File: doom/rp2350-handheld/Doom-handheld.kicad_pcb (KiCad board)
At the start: 2 copper layers, 160 x 100 mm, 42 parts, among them Q1 AO3401A, Q2 FS8205A, SW1 MSK12C02, U1 PIM724, U2 DW01A, U3 BQ24075RGTR

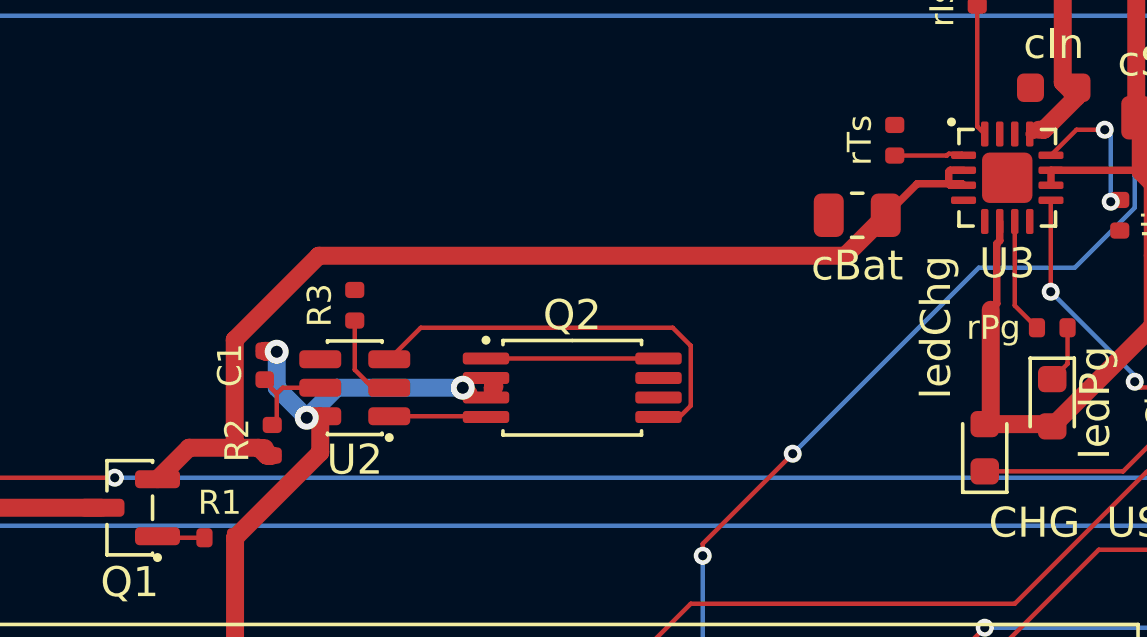
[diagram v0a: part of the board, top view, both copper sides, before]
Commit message: Boards pass check and KiCad 10's DRC again: holes in courtyards, the USB net rename
pcbkit's check now has KiCad 10's pth/npth_inside_courtyard (pcbkit be5b6955), and 13 boards
failed it. KiCad's own DRC (kicad-cli 10) reports the same holes on every one of them.

- Parts that really stand above the holes under them (a screen or a Nano on its sockets, the
  Delta-S02's КМ-6 capacitors flat under its chips, as the factory placed them): a courtyard rule
  for the pair, written to each board's .kicad_dru, so KiCad's DRC agrees.
- Real collisions moved: servo-controller's dial 3 mm up (the Nano's socket pins came out under
  it), c3-pocket's fourth M3 hole from under a cell holder to the top edge's middle, s3-rgb's
  D-pad 2 mm up (a holder's peg came through under the down key).
- v003-emu, c3-pocket, rp2040-tft, rp2350-psram, s3-rgb, teensy41: re-routed for the standard USB
  block's renamed net (usb/raw is usb/vbusIn since pcbkit 2088839e): their tracks still carried
  the old name and shorted the fuse and connector pads.
- p4-touch-7: its board file still had a courtyard for the panel the design gives none (KiCad
  reported 114 courtyard errors); written again.

Measured on the dev host: all 44 registry boards `pcbkit check` complete with 0 errors, and
kicad-cli pcb drc 0 errors on every board.

Claude-Session: https://claude.ai/code/session_018URVYF1YPgyrMNetY9yT1T
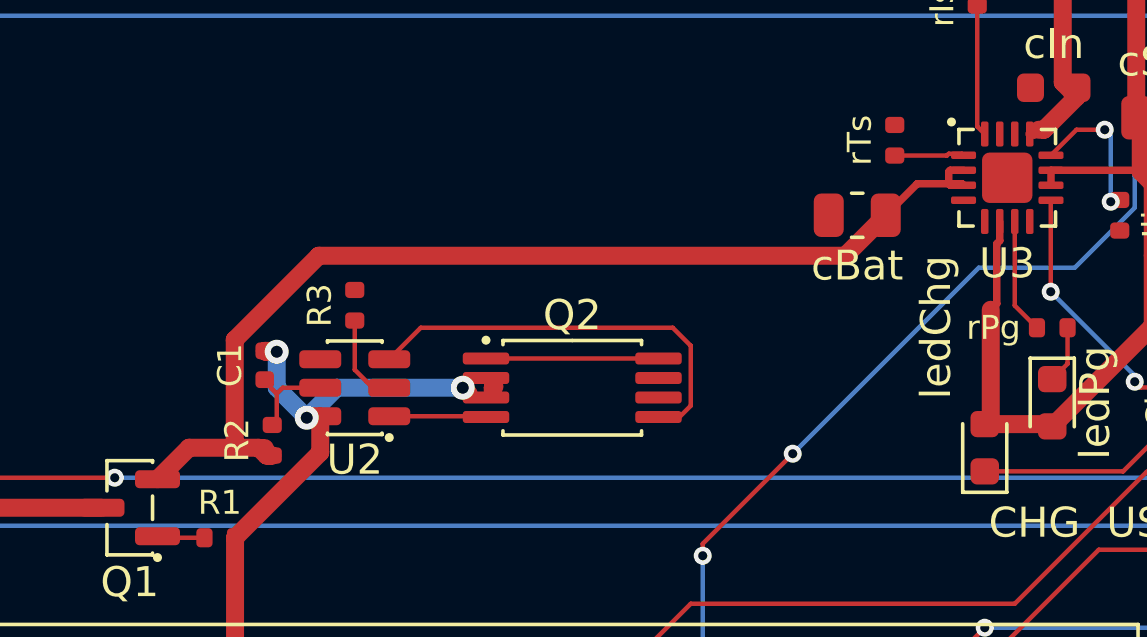
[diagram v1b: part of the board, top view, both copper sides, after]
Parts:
- H1, H2, H3, H4: value (none) -> MountingHole_3.2mm_M3
- logo: value (none) -> Logo_PCBKit_pcbkit.io
- tpGnd, tpRx, tpTx: value (none) -> TestPoint_Round_D1.5mm

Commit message: doom: a resettable fuse per 18650 cell, a 2 % backlight clamp, a 1 A LDO on the S3 boards
The verifier (wiring-parallel-cells) found the two holders of every Doom board directly in parallel:
a cell put in backwards, or one much fuller than the other, drives the other through nothing but
the cells' resistance (about 56-168 A). Each holder's + now reaches BAT_IN through its own 2 A
resettable fuse (Littelfuse 1812L200/16GR, C18198340: 16 V, 100 A interrupting) on new nets
CELL1_P / CELL2_P. Nothing else moved; the boards were re-routed for the new nets.

- s3-rgb: the MT3608 backlight's open-panel clamp was a 28 V 5 % zener (bound 30.0 V against the
  switch's 30 V). It is now two 2 % zeners in series, UDZVTE-1718B + UDZVTE-1710B (27.33-28.56 V;
  LCSC stocks no single 28 V 2 % part). That is under 29.2 V and above the panel's 27.2 V.
- s3-rgb, s3-handheld: TLV75533 (500 mA) -> TLV75733 (1 A, C485517, same DBV pins; sheet from
  SBVS322C), for the ESP32-S3's 500 mA supply peaks (erc-supply-peak).
- c3-pocket, v003-emu: the USB PTC's hold is 750 mA, as the part (nSMD075) is (rating-current).
- pico2-carrier: the CHG/PG LEDs 1.5 mm further from the display's courtyard. rp2350-handheld:
  the logo off the LCD's courtyard and BT1's peg.
- READMEs: the per-cell fuses, the boards already ordered (s3-rgb, JLC W2026102705013253: insert
  the cells one at a time), status and BOM as check and the fab export give them now.

Measured on the dev host (pcbkit 5e0d2cc8): all 11 complete, 0 errors, 0 unrouted. What is left is
erc-rail-name (sent to the verifier as false positives) and full-speed USB pair coupling. The MCU
pins' nets are unchanged on every board, so the firmware and its simulation are unchanged.

Claude-Session: https://claude.ai/code/session_01B3VRfBCg9vAvGVWujVGarr
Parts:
- added F1: PTC 2000mA, Fuse_1812_4532Metric, B.Cu at (128.8, 185.0)
- added F2: PTC 2000mA, Fuse_1812_4532Metric, B.Cu at (128.8, 163.0)
- moved logo 3.35 mm to (177.0, 192.5)
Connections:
- BT1 pad 2: BAT_IN -> CELL1_P
- BT2 pad 2: BAT_IN -> CELL2_P
- down pad 2: DOWN -> GND
- enter pad 2: ENTER -> GND
- fire pad 2: FIRE -> GND
- left pad 2: LEFT -> GND
- menu pad 2: MENU -> GND
- right pad 2: RIGHT -> GND
- strafeLeft pad 2: STRAFE_L -> GND
- strafeRight pad 2: STRAFE_R -> GND
- up pad 2: UP -> GND
- use pad 2: USE -> GND
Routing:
- net BAT_IN: track 93.1 -> 100.8 mm
- net CELL2_P: track 0.00 -> 6.42 mm
- net CELL1_P: track 0.00 -> 6.42 mm

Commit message: boards: 15 boards rebuilt on pcbkit 20ffacdc9 (their pours under the 0.25 mm hole clearance)
Every board checked with main: 17 of 44 failed on hole-clearance (pours filled before fill c6 made
0.25 mm KiCad's hole clearance the default), keepout (holes now sized by the board) or
place-corner. design.run {} on each (placement and routing kept, pours refilled): 15 now complete,
0 errors. Not here: esp32-p4-touch-lcd-7b and p4-touch-7 (a build reroutes their pairs: 21 and 7
unrouted; kept as they were, 2,372 and 919 hole-clearance errors: a refill without a reroute is
needed).

Claude-Session: https://claude.ai/code/session_01BAgp959tApA8aEg85EYgfb
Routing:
- net GND: track 4.88 -> 11.3 mm
- net RX: track 91.1 -> 89.5 mm
